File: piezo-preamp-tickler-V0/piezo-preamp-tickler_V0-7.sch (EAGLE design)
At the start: 22 parts, among them IC1 TLC272, Q4 2N5484

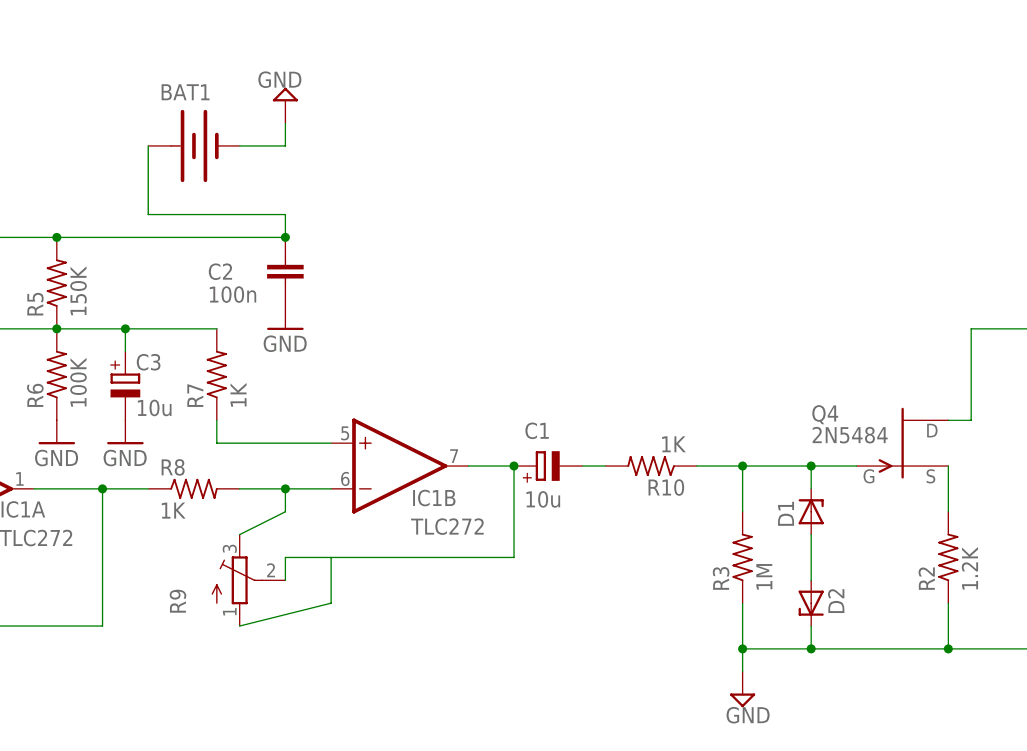
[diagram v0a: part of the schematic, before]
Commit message: On/Off Added, mounting holes added, HP Jacks Mirrored
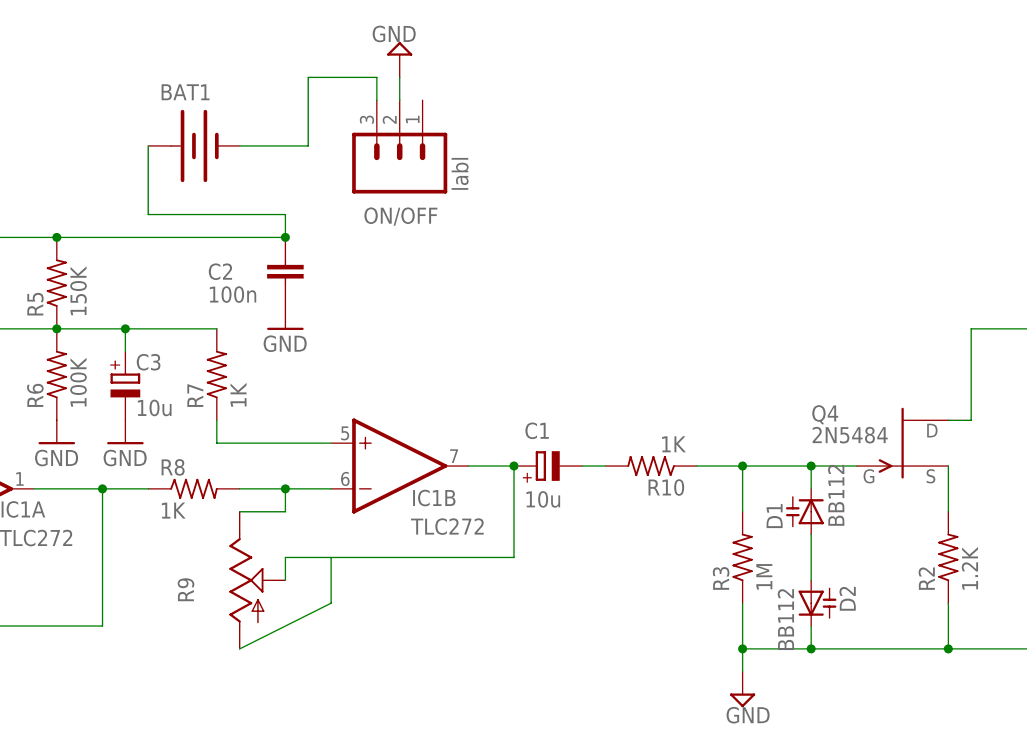
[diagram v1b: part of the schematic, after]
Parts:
- added ON/OFF: labl, Daniel:M03SINGLE-POLE-DOUBLE-THROW
- D1, D2: value 1N821 -> BB112; device diode:1N821 -> diode:BB112
- INPUT-SELECT: device SparkFun-Connectors:M03LOCK -> Daniel:M03SINGLE-POLE-DOUBLE-THROW
- R9: device adafruit:TRIMPOT3386 -> Daniel:TRIM3386
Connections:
- new net N$2: BAT1.-, ON/OFF.3
- net GND: now also ON/OFF.2; no longer BAT1.-

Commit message: minor changes to tickler board v0.7
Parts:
- renumbered IN to PIEZO
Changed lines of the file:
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@@
 <?xml version="1.0" encoding="utf-8"?>
 <!DOCTYPE eagle SYSTEM "eagle.dtd">
-<eagle version="7.5.0">
+<eagle version="7.6.0">
 <drawing>
 <settings>
@@
 <grid distance="0.1" unitdist="inch" unit="inch" style="lines" multiple="1" display="no" altdistance="0.01" altunitdist="inch" altunit="inch"/>
 <layers>
-<layer number="1" name="Top" color="4" fill="1" visible="yes" active="no"/>
-<layer number="16" name="Bottom" color="1" fill="1" visible="yes" active="no"/>
-<layer number="17" name="Pads" color="2" fill="1" visible="yes" active="no"/>
-<layer number="18" name="Vias" color="2" fill="1" visible="yes" active="no"/>
-<layer number="19" name="Unrouted" color="6" fill="1" visible="yes" active="no"/>
-<layer number="20" name="Dimension" color="15" fill="1" visible="yes" active="no"/>
-<layer number="21" name="tPlace" color="7" fill="1" visible="yes" active="no"/>
-<layer number="22" name="bPlace" color="7" fill="1" visible="yes" active="no"/>
-<layer number="23" name="tOrigins" color="15" fill="1" visible="yes" active="no"/>
-<layer number="24" name="bOrigins" color="15" fill="1" visible="yes" active="no"/>
-<layer number="25" name="tNames" color="7" fill="1" visible="yes" active="no"/>
-<layer number="26" name="bNames" color="7" fill="1" visible="yes" active="no"/>
-<layer number="27" name="tValues" color="7" fill="1" visible="yes" active="no"/>
-<layer number="28" name="bValues" color="7" fill="1" visible="yes" active="no"/>
+<layer number="1" name="Top" color="4" fill="1" visible="no" active="no"/>
+<layer number="16" name="Bottom" color="1" fill="1" visible="no" active="no"/>
+<layer number="17" name="Pads" color="2" fill="1" visible="no" active="no"/>
+<layer number="18" name="Vias" color="2" fill="1" visible="no" active="no"/>
+<layer number="19" name="Unrouted" color="6" fill="1" visible="no" active="no"/>
+<layer number="20" name="Dimension" color="15" fill="1" visible="no" active="no"/>
+<layer number="21" name="tPlace" color="7" fill="1" visible="no" active="no"/>
+<layer number="22" name="bPlace" color="7" fill="1" visible="no" active="no"/>
+<layer number="23" name="tOrigins" color="15" fill="1" visible="no" active="no"/>
+<layer number="24" name="bOrigins" color="15" fill="1" visible="no" active="no"/>
+<layer number="25" name="tNames" color="7" fill="1" visible="no" active="no"/>
+<layer number="26" name="bNames" color="7" fill="1" visible="no" active="no"/>
+<layer number="27" name="tValues" color="7" fill="1" visible="no" active="no"/>
+<layer number="28" name="bValues" color="7" fill="1" visible="no" active="no"/>
 <layer number="29" name="tStop" color="7" fill="3" visible="no" active="no"/>
 <layer number="30" name="bStop" color="7" fill="6" visible="no" active="no"/>
@@
 <layer number="35" name="tGlue" color="7" fill="4" visible="no" active="no"/>
 <layer number="36" name="bGlue" color="7" fill="5" visible="no" active="no"/>
-<layer number="37" name="tTest" color="7" fill="1" visible="yes" active="no"/>
-<layer number="38" name="bTest" color="7" fill="1" visible="yes" active="no"/>
+<layer number="37" name="tTest" color="7" fill="1" visible="no" active="no"/>
+<layer number="38" name="bTest" color="7" fill="1" visible="no" active="no"/>
 <layer number="39" name="tKeepout" color="4" fill="11" visible="no" active="no"/>
 <layer number="40" name="bKeepout" color="1" fill="11" visible="no" active="no"/>
@@
 <layer number="44" name="Drills" color="7" fill="1" visible="no" active="no"/>
 <layer number="45" name="Holes" color="7" fill="1" visible="no" active="no"/>
-<layer number="46" name="Milling" color="3" fill="1" visible="yes" active="no"/>
-<layer number="47" name="Measures" color="7" fill="1" visible="yes" active="no"/>
-<layer number="48" name="Document" color="7" fill="1" visible="yes" active="no"/>
-<layer number="49" name="Reference" color="7" fill="1" visible="yes" active="no"/>
-<layer number="50" name="dxf" color="7" fill="1" visible="yes" active="no"/>
-<layer number="51" name="tDocu" color="7" fill="1" visible="yes" active="no"/>
-<layer number="52" name="bDocu" color="7" fill="1" visible="yes" active="no"/>
-<layer number="53" name="tGND_GNDA" color="7" fill="9" visible="yes" active="no"/>
-<layer number="54" name="bGND_GNDA" color="1" fill="9" visible="yes" active="no"/>
-<layer number="56" name="wert" color="7" fill="1" visible="yes" active="no"/>
-<layer number="57" name="tCAD" color="7" fill="1" visible="yes" active="no"/>
-<layer number="59" name="tCarbon" color="7" fill="1" visible="yes" active="no"/>
-<layer number="60" name="bCarbon" color="7" fill="1" visible="yes" active="no"/>
+<layer number="46" name="Milling" color="3" fill="1" visible="no" active="no"/>
+<layer number="47" name="Measures" color="7" fill="1" visible="no" active="no"/>
+<layer number="48" name="Document" color="7" fill="1" visible="no" active="no"/>
+<layer number="49" name="Reference" color="7" fill="1" visible="no" active="no"/>
+<layer number="50" name="dxf" color="7" fill="1" visible="no" active="no"/>
+<layer number="51" name="tDocu" color="7" fill="1" visible="no" active="no"/>
+<layer number="52" name="bDocu" color="7" fill="1" visible="no" active="no"/>
+<layer number="53" name="tGND_GNDA" color="7" fill="9" visible="no" active="no"/>
+<layer number="54" name="bGND_GNDA" color="1" fill="9" visible="no" active="no"/>
+<layer number="56" name="wert" color="7" fill="1" visible="no" active="no"/>
+<layer number="57" name="tCAD" color="7" fill="1" visible="no" active="no"/>
+<layer number="59" name="tCarbon" color="7" fill="1" visible="no" active="no"/>
+<layer number="60" name="bCarbon" color="7" fill="1" visible="no" active="no"/>
 <layer number="90" name="Modules" color="5" fill="1" visible="yes" active="yes"/>
 <layer number="91" name="Nets" color="2" fill="1" visible="yes" active="yes"/>
@@
 <part name="GND8" library="supply1" deviceset="GND" device=""/>
 <part name="GND4" library="supply1" deviceset="GND" device=""/>
-<part name="IN" library="SparkFun-Connectors" deviceset="M02" device="LOCK"/>
+<part name="PIEZO" library="SparkFun-Connectors" deviceset="M02" device="LOCK"/>
 <part name="R4" library="resistor" deviceset="R-US_" device="0204/2V" value="10K"/>
 <part name="R5" library="resistor" deviceset="R-US_" device="0204/2V" value="150K"/>
@@
 <attribute name="VALUE" x="50.8" y="27.94" size="1.778" layer="96" ratio="12"/>
 </instance>
-<instance part="GND8" gate="1" x="71.12" y="43.18" smashed="yes">
-<attribute name="VALUE" x="68.58" y="40.64" size="1.778" layer="96" ratio="12"/>
+<instance part="GND8" gate="1" x="71.12" y="38.1" smashed="yes">
+<attribute name="VALUE" x="68.58" y="35.56" size="1.778" layer="96" ratio="12"/>
 </instance>
 <instance part="GND4" gate="1" x="35.56" y="15.24" smashed="yes">
 <attribute name="VALUE" x="33.02" y="12.7" size="1.778" layer="96" ratio="12"/>
 </instance>
-<instance part="IN" gate="G$1" x="0" y="27.94"/>
+<instance part="PIEZO" gate="G$1" x="0" y="27.94"/>
 <instance part="R4" gate="G$1" x="22.86" y="38.1" rot="R90"/>
 <instance part="R5" gate="G$1" x="45.72" y="48.26" rot="R90"/>
@@
 <instance part="R8" gate="G$1" x="60.96" y="25.4"/>
 <instance part="R9" gate="G$1" x="66.04" y="15.24"/>
-<instance part="SUPPLY6" gate="GND" x="83.82" y="73.66" rot="R180"/>
+<instance part="SUPPLY6" gate="GND" x="86.36" y="81.28" rot="R180"/>
 <instance part="R2" gate="G$1" x="144.78" y="17.78" rot="R90"/>
 <instance part="R1" gate="G$1" x="157.48" y="17.78" rot="R90"/>
@@
 </instance>
 <instance part="ON/OFF" gate="G$1" x="83.82" y="60.96" smashed="yes" rot="R90">
-<attribute name="VALUE" x="91.44" y="58.42" size="1.778" layer="96" rot="R90"/>
 <attribute name="NAME" x="88.138" y="56.642" size="1.778" layer="95" rot="R180"/>
 </instance>
@@
 <pinref part="C2" gate="G$1" pin="1"/>
 <pinref part="GND8" gate="1" pin="GND"/>
+<wire x1="71.12" y1="40.64" x2="71.12" y2="45.72" width="0.1524" layer="91"/>
 </segment>
 <segment>
@@
 <pinref part="ON/OFF" gate="G$1" pin="2"/>
 <pinref part="SUPPLY6" gate="GND" pin="GND"/>
-<wire x1="83.82" y1="68.58" x2="83.82" y2="71.12" width="0.1524" layer="91"/>
+<wire x1="83.82" y1="68.58" x2="86.36" y2="78.74" width="0.1524" layer="91"/>
 </segment>
 </net>
@@
 <net name="N$8" class="0">
 <segment>
-<pinref part="IN" gate="G$1" pin="2"/>
+<pinref part="PIEZO" gate="G$1" pin="2"/>
 <wire x1="45.72" y1="43.18" x2="22.86" y2="43.18" width="0.1524" layer="91"/>
 <wire x1="22.86" y1="43.18" x2="12.7" y2="43.18" width="0.1524" layer="91"/>
@@
 <net name="N$9" class="0">
 <segment>
-<pinref part="IN" gate="G$1" pin="1"/>
+<pinref part="PIEZO" gate="G$1" pin="1"/>
 <pinref part="IC1" gate="A" pin="+IN"/>
 <wire x1="7.62" y1="27.94" x2="22.86" y2="27.94" width="0.1524" layer="91"/>
